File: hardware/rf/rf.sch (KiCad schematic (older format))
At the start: 45 parts, among them J1 BGT24_Module_Castellations, J2 SMP, J3 SMP, J4 SMP, U1 ECS-2520S33-400, U2 LMX2491, U3 BGT24MTR12

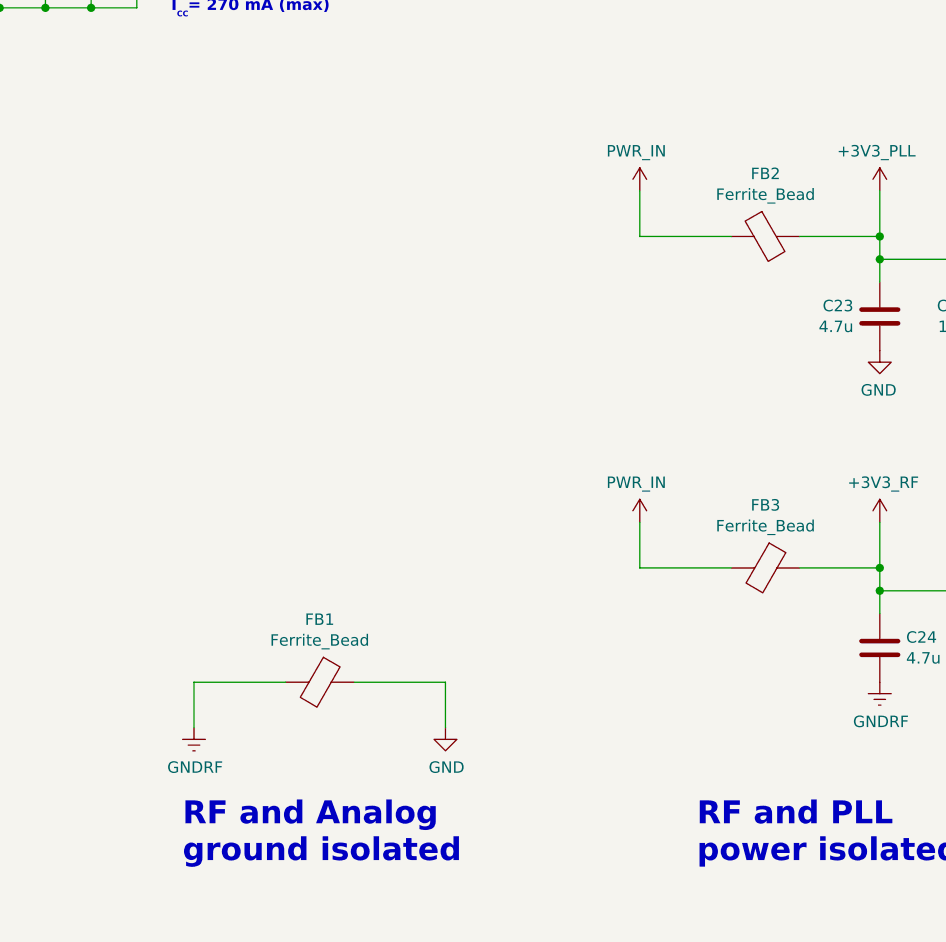
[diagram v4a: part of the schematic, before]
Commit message: BGT24 module final draft layout. Ready for review
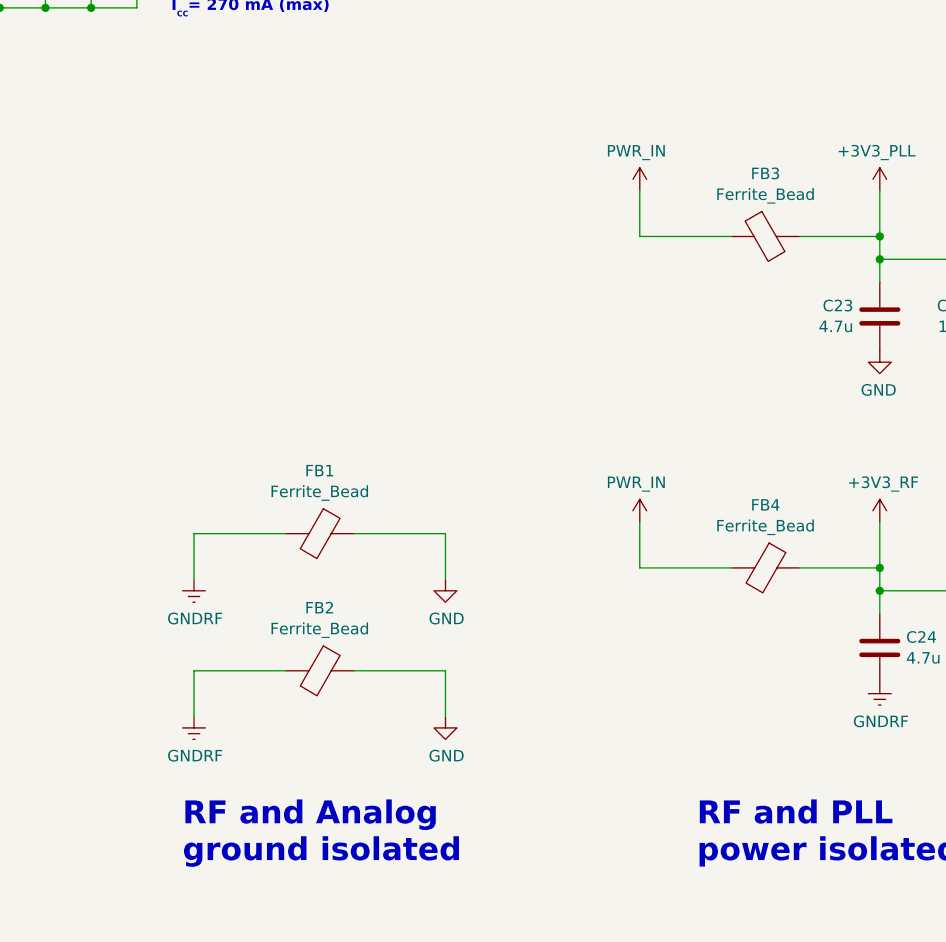
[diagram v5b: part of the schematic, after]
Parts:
- added FB2: Ferrite_Bead, Inductor_SMD:L_0402_1005Metric, symbol Device:Ferrite_Bead
- renumbered FB2 to FB3, FB3 to FB4
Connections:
- net GND: now also FB2.1
- net GNDRF: now also FB2.2
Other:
- moved on the sheet: FB1
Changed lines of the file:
@@
 	10050 7350 9950 7350
 Wire Wire Line
-	12350 7950 12750 7950
-Wire Wire Line
-	12350 8150 12350 7950
-Wire Wire Line
-	13450 7950 13050 7950
-$Comp
-L power:GND #PWR030
+	12350 7300 12750 7300
+Wire Wire Line
+	12350 7500 12350 7300
+Wire Wire Line
+	13450 7300 13050 7300
+$Comp
+L power:GND #PWR031
 U 1 1 5DA51C28
-P 13450 8150
-F 0 "#PWR030" H 13450 7900 50  0001 C CNN
-F 1 "GND" H 13455 7977 50  0000 C CNN
-F 2 "" H 13450 8150 50  0001 C CNN
-F 3 "" H 13450 8150 50  0001 C CNN
-	1    13450 8150
+P 13450 7500
+F 0 "#PWR031" H 13450 7250 50  0001 C CNN
+F 1 "GND" H 13455 7327 50  0000 C CNN
+F 2 "" H 13450 7500 50  0001 C CNN
+F 3 "" H 13450 7500 50  0001 C CNN
+	1    13450 7500
 	1    0    0    -1
 $EndComp
@@
 L Device:Ferrite_Bead FB1
 U 1 1 5DA2D1E7
-P 12900 7950
-F 0 "FB1" V 12626 7950 50  0000 C CNN
-F 1 "Ferrite_Bead" V 12717 7950 50  0000 C CNN
-F 2 "Inductor_SMD:L_0402_1005Metric" V 12830 7950 50  0001 C CNN
-F 3 "~" H 12900 7950 50  0001 C CNN
-	1    12900 7950
+P 12900 7300
+F 0 "FB1" V 12626 7300 50  0000 C CNN
+F 1 "Ferrite_Bead" V 12717 7300 50  0000 C CNN
+F 2 "Inductor_SMD:L_0402_1005Metric" V 12830 7300 50  0001 C CNN
+F 3 "~" H 12900 7300 50  0001 C CNN
+	1    12900 7300
 	0    1    1    0
 $EndComp
@@
 	15850 6200 15850 6100
 $Comp
-L power:GND #PWR037
+L power:GND #PWR039
 U 1 1 5DB1D658
 P 15850 6500
-F 0 "#PWR037" H 15850 6250 50  0001 C CNN
+F 0 "#PWR039" H 15850 6250 50  0001 C CNN
 F 1 "GND" H 15855 6327 50  0000 C CNN
 F 2 "" H 15850 6500 50  0001 C CNN
@@
 $EndComp
 $Comp
-L bloop:+3V3_PLL #PWR033
+L bloop:+3V3_PLL #PWR035
 U 1 1 5DADC61C
 P 15350 5800
-F 0 "#PWR033" H 15350 5650 50  0001 C CNN
+F 0 "#PWR035" H 15350 5650 50  0001 C CNN
 F 1 "+3V3_PLL" H 15365 5973 50  0000 C CNN
 F 2 "" H 15350 5800 50  0001 C CNN
@@
 $EndComp
 $Comp
-L Device:Ferrite_Bead FB2
+L Device:Ferrite_Bead FB3
 U 1 1 5DA5CA3E
 P 14850 6000
-F 0 "FB2" V 14576 6000 50  0000 C CNN
+F 0 "FB3" V 14576 6000 50  0000 C CNN
 F 1 "Ferrite_Bead" V 14667 6000 50  0000 C CNN
 F 2 "Inductor_SMD:L_0402_1005Metric" V 14780 6000 50  0001 C CNN
@@
 $EndComp
 $Comp
-L bloop:PWR_IN #PWR031
+L bloop:PWR_IN #PWR033
 U 1 1 5DADB143
 P 14300 5800
-F 0 "#PWR031" H 14300 5650 50  0001 C CNN
+F 0 "#PWR033" H 14300 5650 50  0001 C CNN
 F 1 "PWR_IN" H 14315 5973 50  0000 C CNN
 F 2 "" H 14300 5800 50  0001 C CNN
@@
 $EndComp
 $Comp
-L power:GND #PWR034
+L power:GND #PWR036
 U 1 1 5E277E12
 P 15350 6500
-F 0 "#PWR034" H 15350 6250 50  0001 C CNN
+F 0 "#PWR036" H 15350 6250 50  0001 C CNN
 F 1 "GND" H 15355 6327 50  0000 C CNN
 F 2 "" H 15350 6500 50  0001 C CNN
@@
 L bloop:GNDRF #PWR029
 U 1 1 5DBF0422
-P 12350 8150
-F 0 "#PWR029" H 12350 7900 50  0001 C CNN
-F 1 "GNDRF" H 12355 7977 50  0000 C CNN
-F 2 "" H 12350 8150 50  0001 C CNN
-F 3 "" H 12350 8150 50  0001 C CNN
-	1    12350 8150
+P 12350 7500
+F 0 "#PWR029" H 12350 7250 50  0001 C CNN
+F 1 "GNDRF" H 12355 7327 50  0000 C CNN
+F 2 "" H 12350 7500 50  0001 C CNN
+F 3 "" H 12350 7500 50  0001 C CNN
+	1    12350 7500
 	1    0    0    -1
 $EndComp
@@
 $EndComp
 $Comp
-L bloop:GNDRF #PWR039
+L bloop:GNDRF #PWR041
 U 1 1 5DC0800F
 P 16000 3250
-F 0 "#PWR039" H 16000 3000 50  0001 C CNN
+F 0 "#PWR041" H 16000 3000 50  0001 C CNN
 F 1 "GNDRF" H 16005 3077 50  0000 C CNN
 F 2 "" H 16000 3250 50  0001 C CNN
@@
 $EndComp
 $Comp
-L bloop:GNDRF #PWR040
+L bloop:GNDRF #PWR042
 U 1 1 5DC08CBA
 P 16000 4000
-F 0 "#PWR040" H 16000 3750 50  0001 C CNN
+F 0 "#PWR042" H 16000 3750 50  0001 C CNN
 F 1 "GNDRF" H 16005 3827 50  0000 C CNN
 F 2 "" H 16000 4000 50  0001 C CNN
@@
 $EndComp
 $Comp
-L bloop:GNDRF #PWR041
+L bloop:GNDRF #PWR043
 U 1 1 5DC095E8
 P 16000 4800
-F 0 "#PWR041" H 16000 4550 50  0001 C CNN
+F 0 "#PWR043" H 16000 4550 50  0001 C CNN
 F 1 "GNDRF" H 16005 4627 50  0000 C CNN
 F 2 "" H 16000 4800 50  0001 C CNN
@@
 	9450 8750 9350 8750
 Wire Wire Line
-	13450 7950 13450 8150
+	13450 7300 13450 7500
 Wire Wire Line
 	9350 8750 9350 8950
@@
 	15350 7250 15350 7450
 $Comp
-L bloop:GNDRF #PWR038
+L bloop:GNDRF #PWR040
 U 1 1 5DBEEA44
 P 15850 7950
-F 0 "#PWR038" H 15850 7700 50  0001 C CNN
+F 0 "#PWR040" H 15850 7700 50  0001 C CNN
 F 1 "GNDRF" H 15855 7777 50  0000 C CNN
 F 2 "" H 15850 7950 50  0001 C CNN
@@
 $EndComp
 $Comp
-L bloop:GNDRF #PWR036
+L bloop:GNDRF #PWR038
 U 1 1 5DBD7E2B
 P 15350 7950
-F 0 "#PWR036" H 15350 7700 50  0001 C CNN
+F 0 "#PWR038" H 15350 7700 50  0001 C CNN
 F 1 "GNDRF" H 15355 7777 50  0000 C CNN
 F 2 "" H 15350 7950 50  0001 C CNN
@@
 $EndComp
 $Comp
-L Device:Ferrite_Bead FB3
+L Device:Ferrite_Bead FB4
 U 1 1 5DAF0710
 P 14850 7450
-F 0 "FB3" V 14576 7450 50  0000 C CNN
+F 0 "FB4" V 14576 7450 50  0000 C CNN
 F 1 "Ferrite_Bead" V 14667 7450 50  0000 C CNN
 F 2 "Inductor_SMD:L_0402_1005Metric" V 14780 7450 50  0001 C CNN
@@
 $EndComp
 $Comp
-L bloop:+3V3_RF #PWR035
+L bloop:+3V3_RF #PWR037
 U 1 1 5DADD4FE
 P 15350 7250
-F 0 "#PWR035" H 15350 7100 50  0001 C CNN
+F 0 "#PWR037" H 15350 7100 50  0001 C CNN
 F 1 "+3V3_RF" H 15365 7423 50  0000 C CNN
 F 2 "" H 15350 7250 50  0001 C CNN
@@
 	14300 7450 14300 7250
 $Comp
-L bloop:PWR_IN #PWR032
+L bloop:PWR_IN #PWR034
 U 1 1 5E404DB8
 P 14300 7250
-F 0 "#PWR032" H 14300 7100 50  0001 C CNN
+F 0 "#PWR034" H 14300 7100 50  0001 C CNN
 F 1 "PWR_IN" H 14315 7423 50  0000 C CNN
 F 2 "" H 14300 7250 50  0001 C CNN
@@
 Wire Wire Line
 	14150 3050 13950 3050
+Wire Wire Line
+	12350 7900 12750 7900
+Wire Wire Line
+	12350 8100 12350 7900
+Wire Wire Line
+	13450 7900 13050 7900
+$Comp
+L power:GND #PWR032
+U 1 1 5DB81C9A
+P 13450 8100
+F 0 "#PWR032" H 13450 7850 50  0001 C CNN
+F 1 "GND" H 13455 7927 50  0000 C CNN
+F 2 "" H 13450 8100 50  0001 C CNN
+F 3 "" H 13450 8100 50  0001 C CNN
+	1    13450 8100
+	1    0    0    -1
+$EndComp
+$Comp
+L Device:Ferrite_Bead FB2
+U 1 1 5DB81CA0
+P 12900 7900
+F 0 "FB2" V 12626 7900 50  0000 C CNN
+F 1 "Ferrite_Bead" V 12717 7900 50  0000 C CNN
+F 2 "Inductor_SMD:L_0402_1005Metric" V 12830 7900 50  0001 C CNN
+F 3 "~" H 12900 7900 50  0001 C CNN
+	1    12900 7900
+	0    1    1    0
+$EndComp
+$Comp
+L bloop:GNDRF #PWR030
+U 1 1 5DB81CA6
+P 12350 8100
+F 0 "#PWR030" H 12350 7850 50  0001 C CNN
+F 1 "GNDRF" H 12355 7927 50  0000 C CNN
+F 2 "" H 12350 8100 50  0001 C CNN
+F 3 "" H 12350 8100 50  0001 C CNN
+	1    12350 8100
+	1    0    0    -1
+$EndComp
+Wire Wire Line
+	13450 7900 13450 8100
 $EndSCHEMATC

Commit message: Layout review edits with Austin. Added BGT24 Module FAB files and started the panel for the module
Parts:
- U2: footprint Package_DFN_QFN:VQFN-24-1EP_4x4mm_P0.5mm_EP2.45x2.45mm_ThermalVias -> Package_DFN_QFN:VQFN-24-1EP_4x4mm_P0.5mm_EP2.45x2.45mm
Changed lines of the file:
@@
 F 0 "U2" H 5650 6350 60  0000 C CNN
 F 1 "LMX2491" H 5650 3500 60  0000 C CNN
-F 2 "Package_DFN_QFN:VQFN-24-1EP_4x4mm_P0.5mm_EP2.45x2.45mm_ThermalVias" H 5650 4500 60  0001 C CNN
+F 2 "Package_DFN_QFN:VQFN-24-1EP_4x4mm_P0.5mm_EP2.45x2.45mm" H 5650 4500 60  0001 C CNN
 F 3 "http://www.ti.com/lit/ds/symlink/lmx2491.pdf" H 5650 4700 60  0001 C CNN
 F 4 "LMX2491RTWR" H 5650 4700 50  0001 C CNN "MPN"
@@
 F 1 "SMP" H 16060 2920 50  0000 L CNN
 F 2 "bloop:85305-0232" H 16000 3050 50  0001 C CNN
-F 3 " ~" H 16000 3050 50  0001 C CNN
+F 3 "https://www.molex.com/molex/products/datasheet.jsp?part=active/0853050232_RF_COAX_CONNECTORS.xml" H 16000 3050 50  0001 C CNN
 	1    16000 3050
 	1    0    0    -1
@@
 F 1 "SMP" H 16060 3670 50  0000 L CNN
 F 2 "bloop:85305-0232" H 16000 3800 50  0001 C CNN
-F 3 " ~" H 16000 3800 50  0001 C CNN
+F 3 "https://www.molex.com/molex/products/datasheet.jsp?part=active/0853050232_RF_COAX_CONNECTORS.xml" H 16000 3800 50  0001 C CNN
 	1    16000 3800
 	1    0    0    -1
@@
 F 1 "SMP" H 16060 4470 50  0000 L CNN
 F 2 "bloop:85305-0232" H 16000 4600 50  0001 C CNN
-F 3 " ~" H 16000 4600 50  0001 C CNN
+F 3 "https://www.molex.com/molex/products/datasheet.jsp?part=active/0853050232_RF_COAX_CONNECTORS.xml" H 16000 4600 50  0001 C CNN
 	1    16000 4600
 	1    0    0    -1

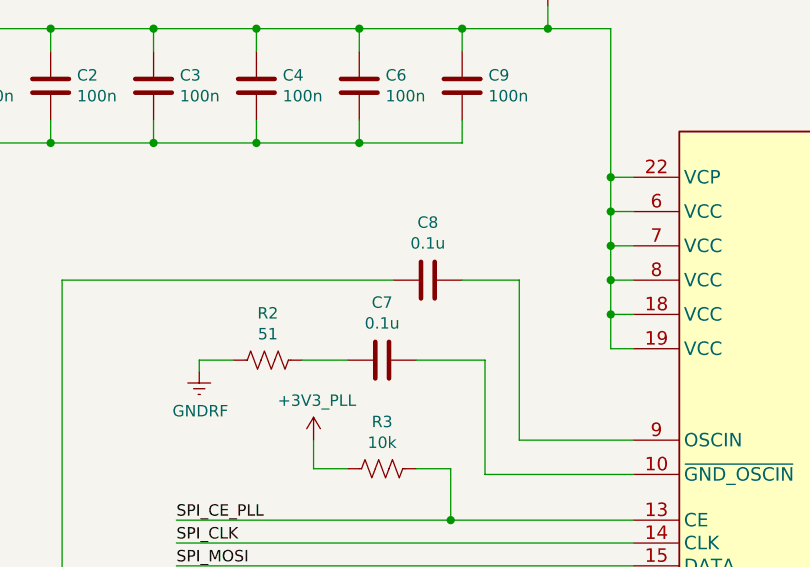
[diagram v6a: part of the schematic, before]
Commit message: Assigned MPNs to components and generated BOM. Small layout edits for changed part footprints
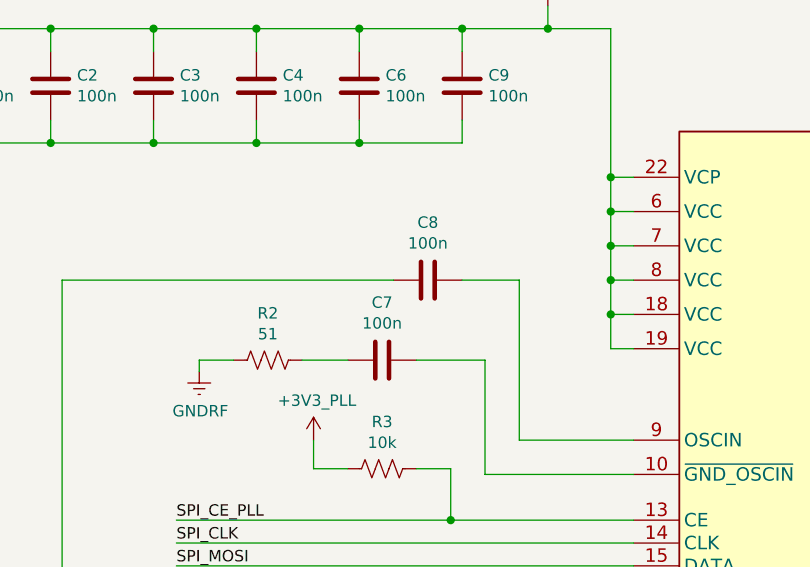
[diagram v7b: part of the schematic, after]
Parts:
- C1, C15, C2, C3, C4, C5, C6, C9: MPN (none) -> GRM033R6YA104KE14D
- C10, C11: MPN (none) -> GCM1555C1H100GA16D
- C12: MPN (none) -> GRM033R61C223KE84D
- C13, C18, C19: MPN (none) -> GRM033R71H102KA12D
- C14: MPN (none) -> GRM033R61C333KE84D
- C17, C25, C26: MPN (none) -> GRM033R71E103KE14D
- C23, C24: MPN (none) -> GRM188R61E475KE11D
- C7, C8: value 0.1u -> 100n; MPN (none) -> GRM033R6YA104KE14D
- FB1, FB2, FB3, FB4: MPN (none) -> MPZ1005S121CT000
- J2, J3, J4: MPN (none) -> 0853050232
- R1, R2: footprint Capacitor_SMD:C_0201_0603Metric -> Resistor_SMD:R_0201_0603Metric; MPN (none) -> ERJ-1GNF51R0C
- R3: footprint Capacitor_SMD:C_0201_0603Metric -> Resistor_SMD:R_0201_0603Metric; MPN (none) -> ERJ-1GNF1002C
- R4: footprint Capacitor_SMD:C_0402_1005Metric -> Resistor_SMD:R_0201_0603Metric; MPN (none) -> ERJ-1GNF51R0C
- R5: footprint Capacitor_SMD:C_0201_0603Metric -> Resistor_SMD:R_0201_0603Metric; MPN (none) -> ERJ-1GNJ121C
- R6: footprint Capacitor_SMD:C_0201_0603Metric -> Resistor_SMD:R_0201_0603Metric; MPN (none) -> ERJ-1GNF8200C
- R7: footprint Capacitor_SMD:C_0201_0603Metric -> Resistor_SMD:R_0201_0603Metric; MPN (none) -> ERJ-1GNF1000C
